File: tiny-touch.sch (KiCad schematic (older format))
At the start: 118 parts, among them IC1 STM32F072VBT6, U1 MCP1700-3002E_SOT23, U2 SRV05-4

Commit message: Begin PCB layout
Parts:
- C1, C2: footprint 0805 -> Capacitor_SMD:C_0603_1608Metric_Pad1.05x0.95mm_HandSolder
- C10, C11, C3, C4, C5, C6, C7, C8, C9: renamed from C?; footprint 0805 -> Capacitor_SMD:C_0603_1608Metric_Pad1.05x0.95mm_HandSolder
- D1: footprint PMDU -> ckeys:PMDU
- D2: renamed from D?; footprint Diode_THT:D_DO-35_SOD27_P7.62mm_Horizontal -> Diode_SMD:D_SOD-323_HandSoldering
- H1: footprint (none) -> ckeys:microbit-clamp-hole-pad
- PAD13, PAD14, PAD15: renamed from blank; footprint ckeys:Tiny-Touch-Pad -> ckeys:Tiny-Touch-Pad-2u
- PAD16, PAD85: renamed from space; footprint ckeys:Tiny-Touch-Pad -> ckeys:Tiny-Touch-Pad-3u
- PAD17: renamed from up; footprint ckeys:Tiny-Touch-Pad -> ckeys:Tiny-Touch-Pad-1.75u
- PAD18: renamed from down; footprint ckeys:Tiny-Touch-Pad -> ckeys:Tiny-Touch-Pad-1.75u
- PAD19: renamed from right; footprint ckeys:Tiny-Touch-Pad -> ckeys:Tiny-Touch-Pad-1.75u
- PAD20: renamed from left; footprint ckeys:Tiny-Touch-Pad -> ckeys:Tiny-Touch-Pad-1.75u
- PAD21: renamed from esc; footprint ckeys:Tiny-Touch-Pad -> ckeys:Tiny-Touch-Pad-2u
- PAD22, PAD42: renamed from tab; footprint ckeys:Tiny-Touch-Pad -> ckeys:Tiny-Touch-Pad-1.5u
- PAD23: renamed from caps; footprint ckeys:Tiny-Touch-Pad -> ckeys:Tiny-Touch-Pad-1.5u
- PAD24, PAD68: renamed from shift; footprint ckeys:Tiny-Touch-Pad -> ckeys:Tiny-Touch-Pad-2.25u
- PAD25: renamed from enter; footprint ckeys:Tiny-Touch-Pad -> ckeys:Tiny-Touch-Pad-2.25u
- PAD26: renamed from backspace; footprint ckeys:Tiny-Touch-Pad -> ckeys:Tiny-Touch-Pad-2.25u
- PAD27: renamed from delete; footprint ckeys:Tiny-Touch-Pad -> ckeys:Tiny-Touch-Pad-2.25u
- PAD54: renamed from ]; footprint ckeys:Tiny-Touch-Pad -> ckeys:Tiny-Touch-Pad-1.5u
- PAD55: renamed from caps; footprint ckeys:Tiny-Touch-Pad -> ckeys:Tiny-Touch-Pad-1.75u
- PAD67: renamed from enter; footprint ckeys:Tiny-Touch-Pad -> ckeys:Tiny-Touch-Pad-1.25u
- PAD79: renamed from shift; footprint ckeys:Tiny-Touch-Pad -> ckeys:Tiny-Touch-Pad-1.75u
- PF1: renamed from PF?; footprint (none) -> Fuse:Fuse_1206_3216Metric_Pad1.42x1.75mm_HandSolder
- Q1: renamed from Q?; footprint (none) -> ckeys:SOT65P210X100-3N
- R1, R2: footprint 0805 -> Resistor_SMD:R_0603_1608Metric_Pad1.05x0.95mm_HandSolder
- R3, R4, R5, R6: renamed from R?; footprint 0805 -> Resistor_SMD:R_0603_1608Metric_Pad1.05x0.95mm_HandSolder
- SW1: renamed from SW?; footprint (none) -> Button_Switch_SMD:SW_Push_1P1T_NO_6x6mm_H9.5mm
- USB1: footprint (none) -> Type-C:HRO-TYPE-C-31-M-12-HandSoldering
- renumbered F1 to PAD1, F10 to PAD10, F11 to PAD11, F12 to PAD12, F2 to PAD2, ` to PAD28, num1 to PAD29, F3 to PAD3, num2 to PAD30, num3 to PAD31, num4 to PAD32, num5 to PAD33, num6 to PAD34, num7 to PAD35, num8 to PAD36, num9 to PAD37, num0 to PAD38, - to PAD39, F4 to PAD4, = to PAD40, \ to PAD41, q to PAD43, w to PAD44, e to PAD45, r to PAD46, t to PAD47, y to PAD48, u to PAD49, F5 to PAD5, i to PAD50, o to PAD51, p to PAD52, [ to PAD53, a to PAD56, s to PAD57, d to PAD58, f to PAD59, F6 to PAD6, g to PAD60, h to PAD61, j to PAD62, k to PAD63, l to PAD64, ; to PAD65, ' to PAD66, z to PAD69, F7 to PAD7, x to PAD70, c to PAD71, v to PAD72, b to PAD73, n to PAD74, m to PAD75, , to PAD76, . to PAD77, / to PAD78, F8 to PAD8, hyper to PAD80, super to PAD81, ctrl to PAD82, win to PAD83, alt to PAD84, alt to PAD86, win to PAD87, menu to PAD88, ctrl to PAD89, F9 to PAD9, super to PAD90, hyper to PAD91

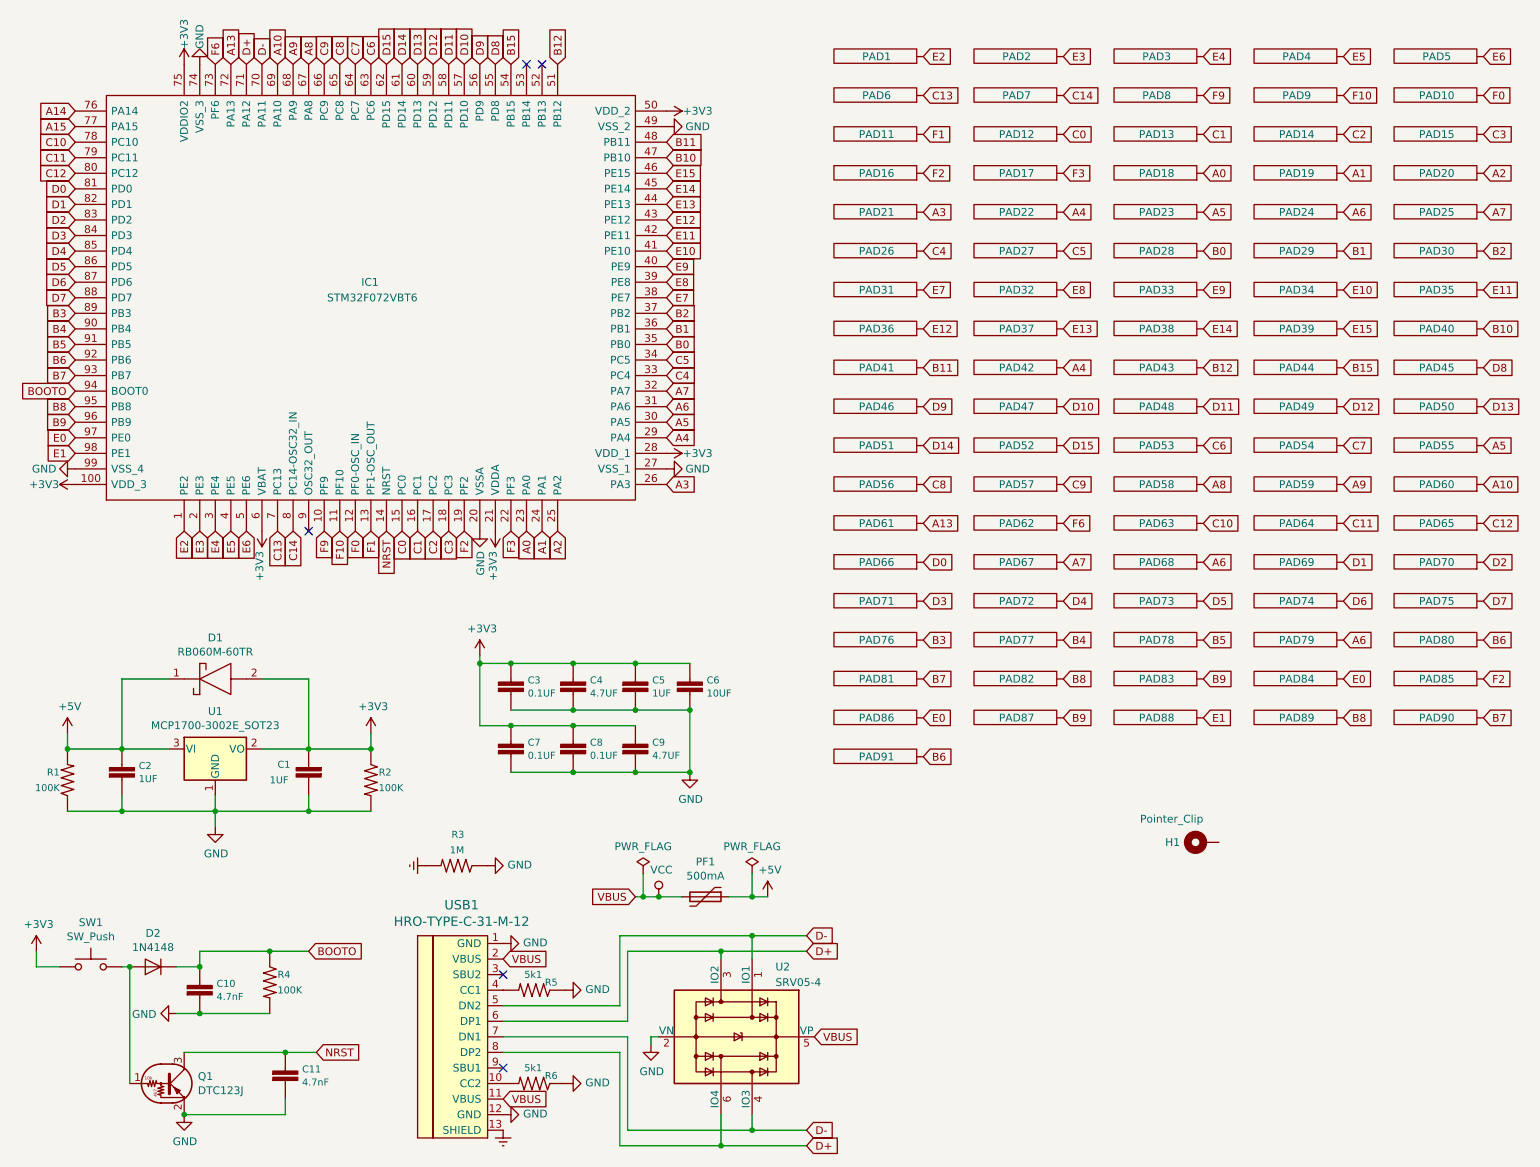
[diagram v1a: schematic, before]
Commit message: Fixed small issues and connected all pins
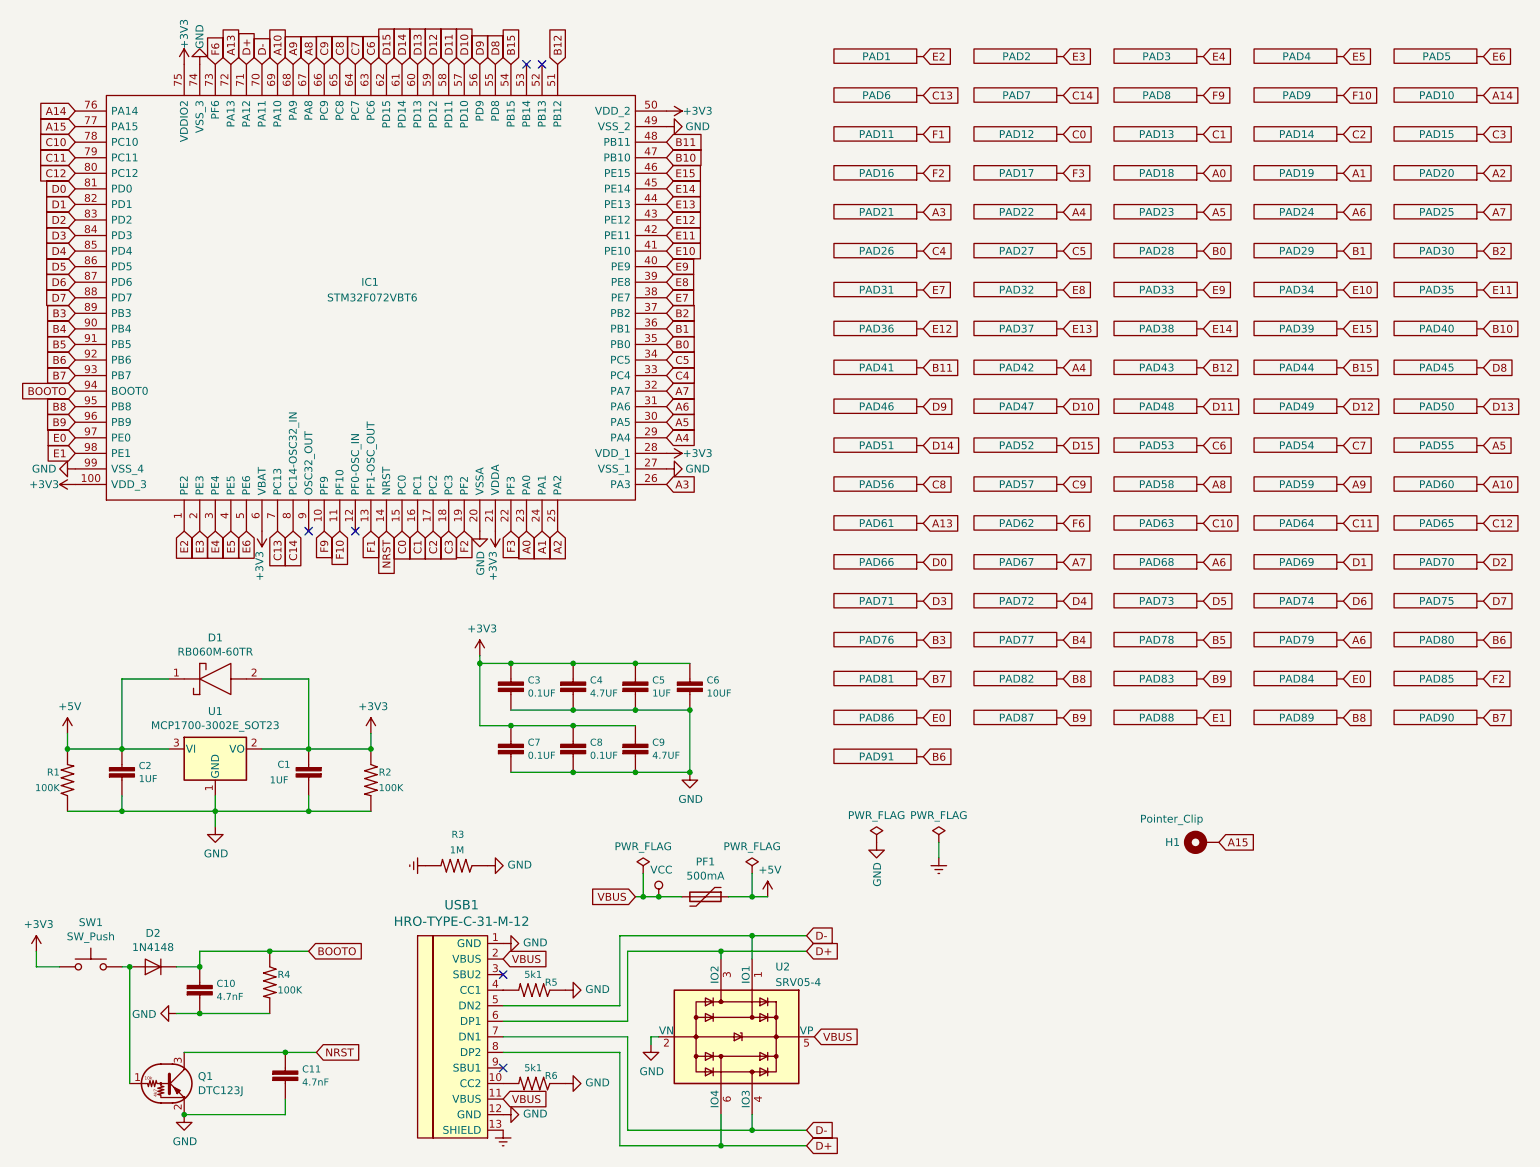
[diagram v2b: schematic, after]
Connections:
- net A14: now also PAD10.1
- net A15: now also H1.1
- net F0: no longer names the net of IC1.12 (PF0-OSC_IN)
- net F0: no longer PAD10.1
- no-connect marks 5 -> 6
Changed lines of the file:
@@
 	0    -1   -1   0
 $EndComp
-Text GLabel 3600 6650 2    50   Input ~ 0
-VBUS
 NoConn ~ 3600 6750
 NoConn ~ 3600 7350
@@
 Text GLabel 2550 3900 3    50   Input ~ 0
 F10
-Text GLabel 2650 3900 3    50   Input ~ 0
-F0
-Text GLabel 2750 3900 3    50   Input ~ 0
-F1
 Text GLabel 2950 3900 3    50   Input ~ 0
 C0
@@
 Text GLabel 3950 900  1    50   Input ~ 0
 B12
-Text GLabel 850  1200 0    50   Input ~ 0
-A14
 Text GLabel 850  1500 0    50   Input ~ 0
 C11
@@
 F10
 Text GLabel 9900 1100 2    50   Input ~ 0
-F0
-Text GLabel 6300 1350 2    50   Input ~ 0
-F1
+A14
 Text GLabel 8100 1350 2    50   Input ~ 0
 C1
@@
 Text GLabel 9000 5100 2    50   Input ~ 0
 B8
+Text GLabel 8200 5900 2    50   Input ~ 0
+A15
+Text GLabel 6300 1350 2    50   Input ~ 0
+F1
+Text GLabel 2750 3900 3    50   Input ~ 0
+F1
+NoConn ~ 2650 3900
+Text GLabel 850  1200 0    50   Input ~ 0
+A14
+Text GLabel 3600 6650 2    50   Input ~ 0
+VBUS
+$Comp
+L power:PWR_FLAG #FLG0103
+U 1 1 5F24BC94
+P 6000 5900
+F 0 "#FLG0103" H 6000 5975 50  0001 C CNN
+F 1 "PWR_FLAG" H 6000 6073 50  0000 C CNN
+F 2 "" H 6000 5900 50  0001 C CNN
+F 3 "~" H 6000 5900 50  0001 C CNN
+	1    6000 5900
+	1    0    0    -1
+$EndComp
+$Comp
+L power:GND #PWR0130
+U 1 1 5F24C2D8
+P 6000 5900
+F 0 "#PWR0130" H 6000 5650 50  0001 C CNN
+F 1 "GND" V 6005 5772 50  0000 R CNN
+F 2 "" H 6000 5900 50  0001 C CNN
+F 3 "" H 6000 5900 50  0001 C CNN
+	1    6000 5900
+	1    0    0    -1
+$EndComp
+$Comp
+L power:GNDREF #PWR0131
+U 1 1 5F24CB0B
+P 6400 6000
+F 0 "#PWR0131" H 6400 5750 50  0001 C CNN
+F 1 "GNDREF" V 6405 5872 50  0001 R CNN
+F 2 "" H 6400 6000 50  0001 C CNN
+F 3 "" H 6400 6000 50  0001 C CNN
+	1    6400 6000
+	1    0    0    -1
+$EndComp
+$Comp
+L power:PWR_FLAG #FLG0104
+U 1 1 5F24DC68
+P 6400 5900
+F 0 "#FLG0104" H 6400 5975 50  0001 C CNN
+F 1 "PWR_FLAG" H 6400 6073 50  0000 C CNN
+F 2 "" H 6400 5900 50  0001 C CNN
+F 3 "~" H 6400 5900 50  0001 C CNN
+	1    6400 5900
+	1    0    0    -1
+$EndComp
+Wire Wire Line
+	6400 5900 6400 6000
 $EndSCHEMATC
